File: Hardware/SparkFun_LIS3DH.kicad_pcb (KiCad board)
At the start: 2 copper layers, 25.4 x 25.4 mm, 53 parts, among them J1 Conn_01x02, J2 Conn_01x05, J3 Qwiic_RA, J4 I2C, J5 Qwiic_RA, U1 LIS3DH

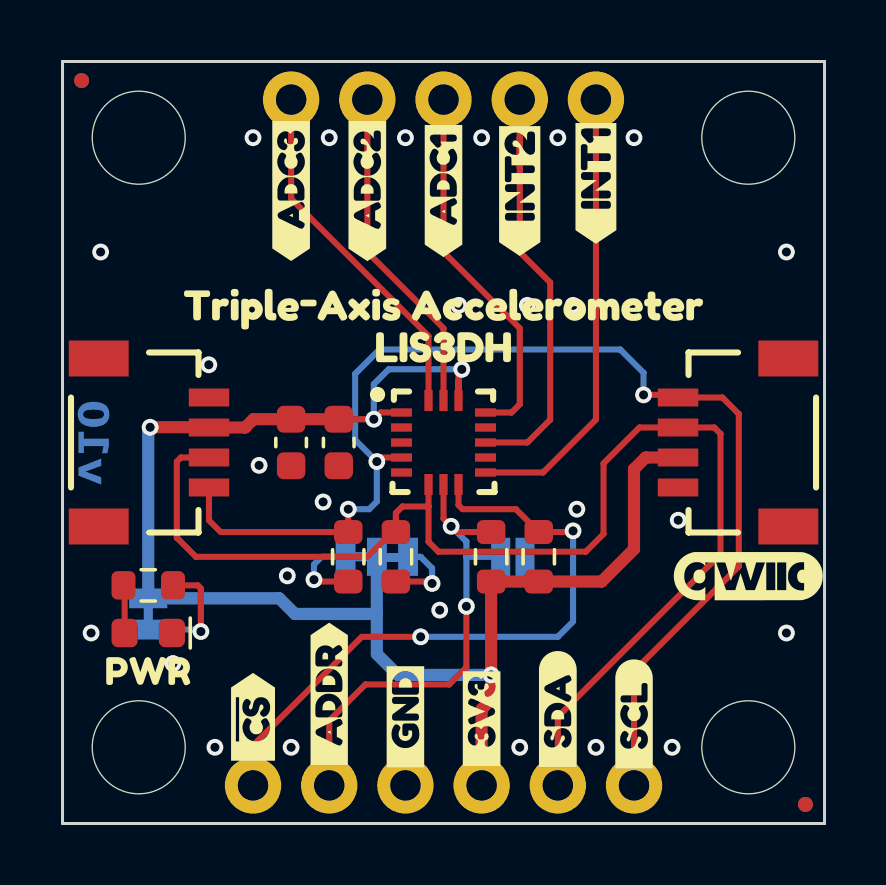
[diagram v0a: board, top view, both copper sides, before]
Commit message: Aligns the PTH for breadboard-ability
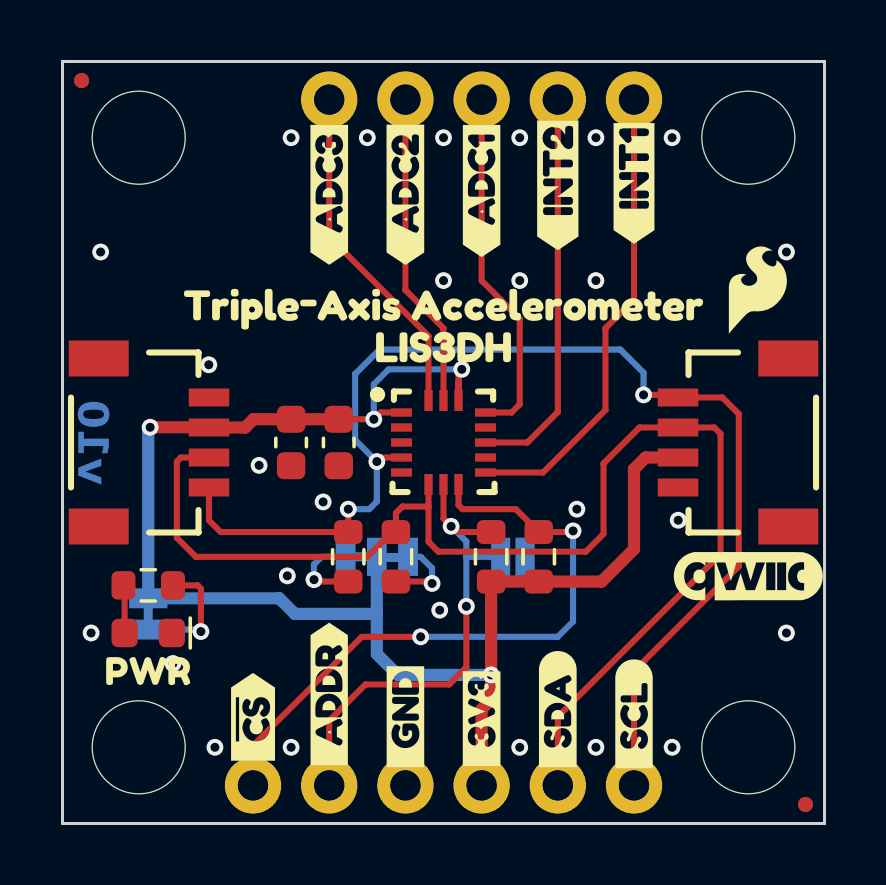
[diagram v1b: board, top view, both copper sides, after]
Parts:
- added G***: Flame, SparkFun-Aesthetic:SparkFun_Flame_3mm, F.Cu at (146.4, 93.0)
- moved kibuzzard-683879AC 1.28 mm to (139.8, 89.5)
- moved kibuzzard-68387A37 1.28 mm to (134.7, 89.9)
- moved kibuzzard-68387A3F 1.28 mm to (132.2, 89.9)
- moved J2 1.27 mm to (142.3, 86.7)
- moved kibuzzard-6838798C 1.27 mm to (142.3, 89.5)
- moved kibuzzard-68387A29 1.27 mm to (137.2, 89.7)
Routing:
- net INT1: track 14.6 -> 13.2 mm
- net INT2: track 15.1 -> 15.6 mm
- net ADC2: track 11.1 -> 10.6 mm
- net ADC1: track 11.9 -> 11.4 mm
- net ADC3: track 12.5 -> 11.9 mm

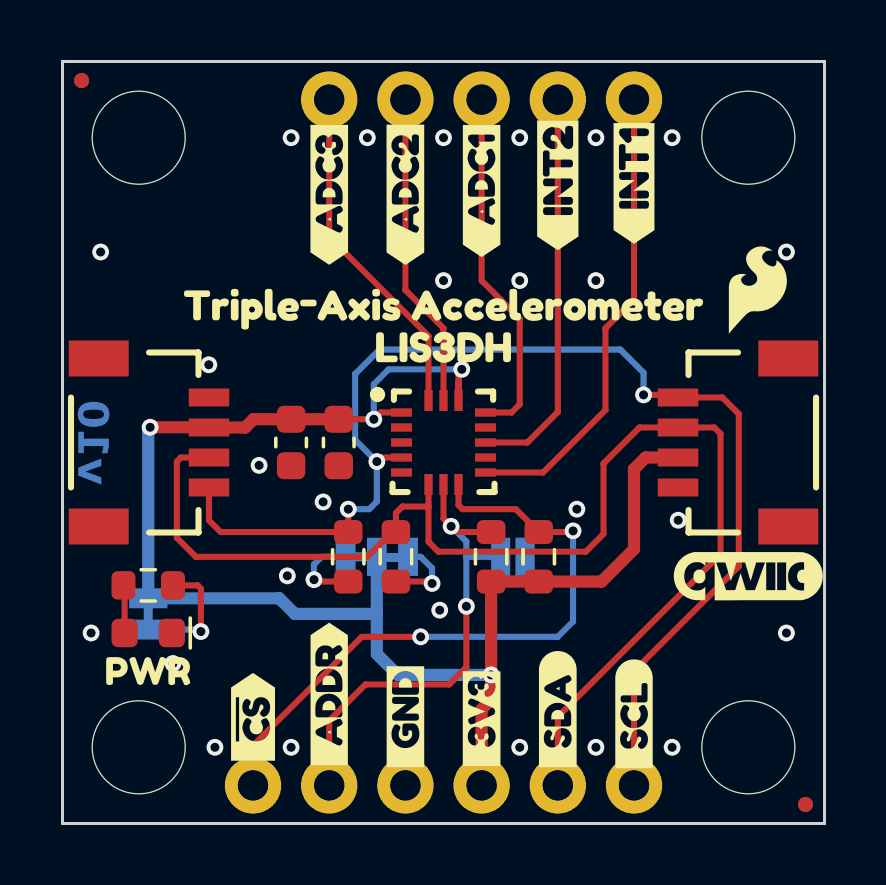
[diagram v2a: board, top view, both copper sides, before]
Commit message: Finishes schematic for mini sized version
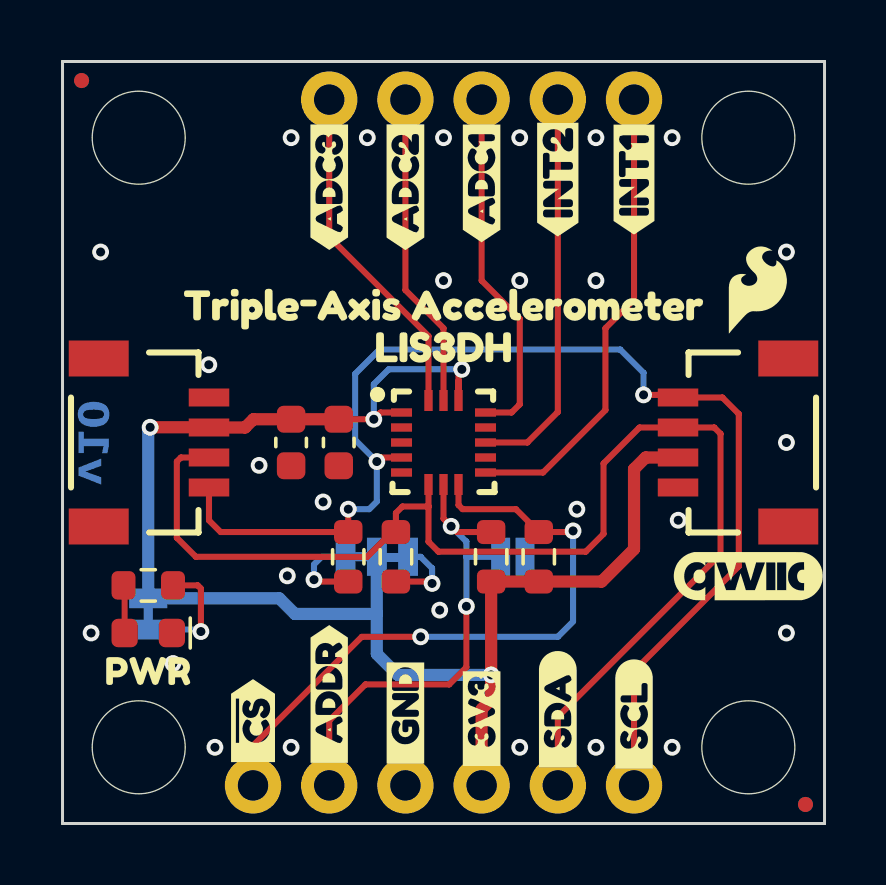
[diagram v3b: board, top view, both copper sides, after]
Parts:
- removed kibuzzard-67BF7C99: G***, kibuzzard-67BF7C99
- removed kibuzzard-67BF7CAB: G***, kibuzzard-67BF7CAB
- removed kibuzzard-67BF7CFE: G***, kibuzzard-67BF7CFE
- removed kibuzzard-67BF7D12: G***, kibuzzard-67BF7D12
- removed kibuzzard-67BF7F2F: G***, kibuzzard-67BF7F2F
- removed kibuzzard-6838798C: G***, kibuzzard-6838798C
- removed kibuzzard-683879AC: G***, kibuzzard-683879AC
- removed kibuzzard-68387A29: G***, kibuzzard-68387A29
- removed kibuzzard-68387A37: G***, kibuzzard-68387A37
- removed kibuzzard-68387A3F: G***, kibuzzard-68387A3F
- removed kibuzzard-68387A66: G***, kibuzzard-68387A66
- removed kibuzzard-68387A76: G***, kibuzzard-68387A76
- added kibuzzard-6838B6EB: G***, kibuzzard-6838B6EB, B.Cu at (141.4, 101.9)
- added kibuzzard-6838B72C: G***, kibuzzard-6838B72C, F.Cu at (139.8, 89.3)
- added kibuzzard-6838B739: G***, kibuzzard-6838B739, F.Cu at (137.2, 89.5)
- added kibuzzard-6838B744: G***, kibuzzard-6838B744, F.Cu at (134.7, 89.6)
- added kibuzzard-6838B74C: G***, kibuzzard-6838B74C, F.Cu at (132.2, 89.6)
- added kibuzzard-6838B753: G***, kibuzzard-6838B753, F.Cu at (142.3, 89.3)
- added kibuzzard-6838B970: G***, kibuzzard-6838B970, F.Cu at (129.6, 107.4)
- added kibuzzard-6838B970: G***, kibuzzard-6838B970, B.Cu at (129.7, 107.4)
- added kibuzzard-6838B976: G***, kibuzzard-6838B976, F.Cu at (132.2, 106.5)
- added kibuzzard-6838B976: G***, kibuzzard-6838B976, B.Cu at (132.2, 106.5)
- added kibuzzard-6838B97C: G***, kibuzzard-6838B97C, F.Cu at (134.7, 107.1)
- added kibuzzard-6838B980: G***, kibuzzard-6838B980, F.Cu at (137.2, 107.3)
- added kibuzzard-6838B984: G***, kibuzzard-6838B984, F.Cu at (139.8, 107.0)
- added kibuzzard-6838B988: G***, kibuzzard-6838B988, F.Cu at (142.3, 107.2)
- added kibuzzard-6838BA05: G***, kibuzzard-6838BA05, B.Cu at (139.8, 89.3)
- added kibuzzard-6838BA16: G***, kibuzzard-6838BA16, B.Cu at (142.3, 89.3)
- added kibuzzard-6838BA22: G***, kibuzzard-6838BA22, B.Cu at (132.2, 89.5)
- added kibuzzard-6838BA4A: G***, kibuzzard-6838BA4A, B.Cu at (134.7, 89.3)
- added kibuzzard-6838BA57: G***, kibuzzard-6838BA57, B.Cu at (137.2, 89.6)
- added kibuzzard-6838BBAA: G***, kibuzzard-6838BBAA, B.Cu at (142.3, 107.2)
- moved kibuzzard-67D9D97F 0.19 mm to (130.8, 101.9)
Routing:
- net GND: vias 26 -> 27

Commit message: Fixes some silk
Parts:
- removed kibuzzard-67BF7EBF: G***, kibuzzard-67BF7EBF
- removed kibuzzard-67BF7ED9: G***, kibuzzard-67BF7ED9
- removed kibuzzard-67BF7F13: G***, kibuzzard-67BF7F13
- removed kibuzzard-6838B739: G***, kibuzzard-6838B739
- removed the kibuzzard-6838B970 at (129.7, 107.4)
- removed the kibuzzard-6838B976 at (132.2, 106.5)
- removed kibuzzard-6838BA57: G***, kibuzzard-6838BA57
- added kibuzzard-68489282: G***, kibuzzard-68489282, B.Cu at (139.8, 107.0)
- added kibuzzard-6848928D: G***, kibuzzard-6848928D, B.Cu at (137.2, 107.3)
- added kibuzzard-68489296: G***, kibuzzard-68489296, B.Cu at (134.7, 107.2)
- added kibuzzard-684892AC: G***, kibuzzard-684892AC, B.Cu at (132.2, 106.5)
- added kibuzzard-684892BE: G***, kibuzzard-684892BE, B.Cu at (129.6, 107.4)
- added kibuzzard-68489319: G***, kibuzzard-68489319, F.Cu at (137.2, 89.5)
- added kibuzzard-68489323: G***, kibuzzard-68489323, B.Cu at (137.2, 89.5)
- moved G*** 1.80 mm to (135.7, 93.5)
- moved kibuzzard-6837731A 0.25 mm to (136.0, 98.4)

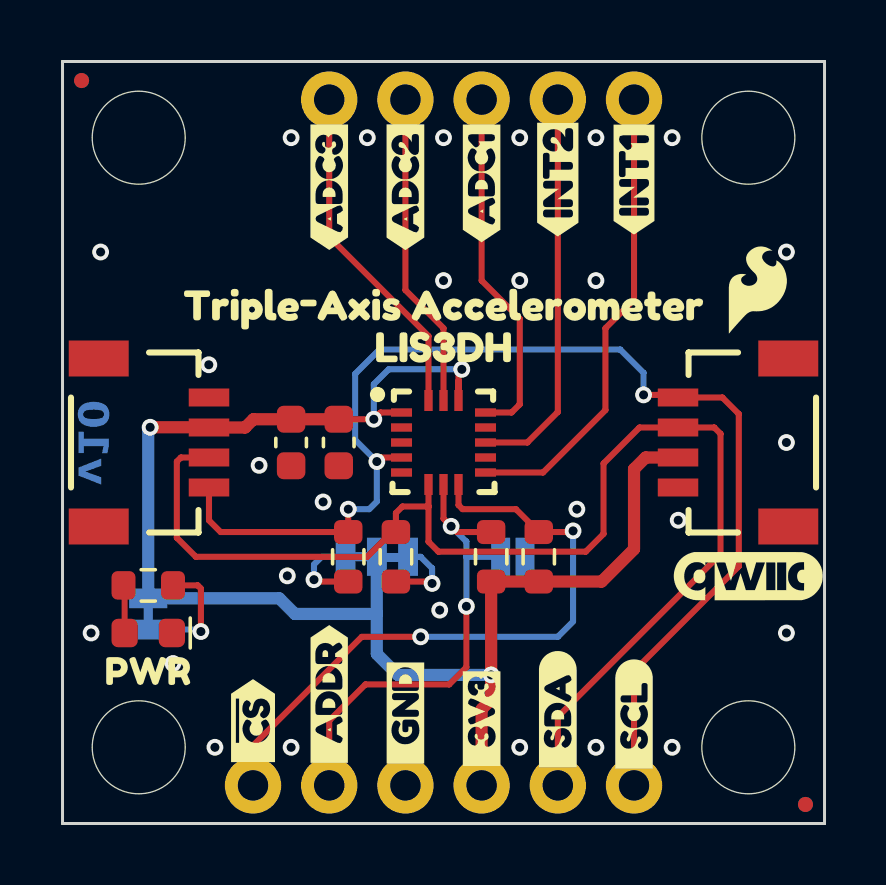
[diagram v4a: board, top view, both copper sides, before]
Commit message: Fixes LED silk
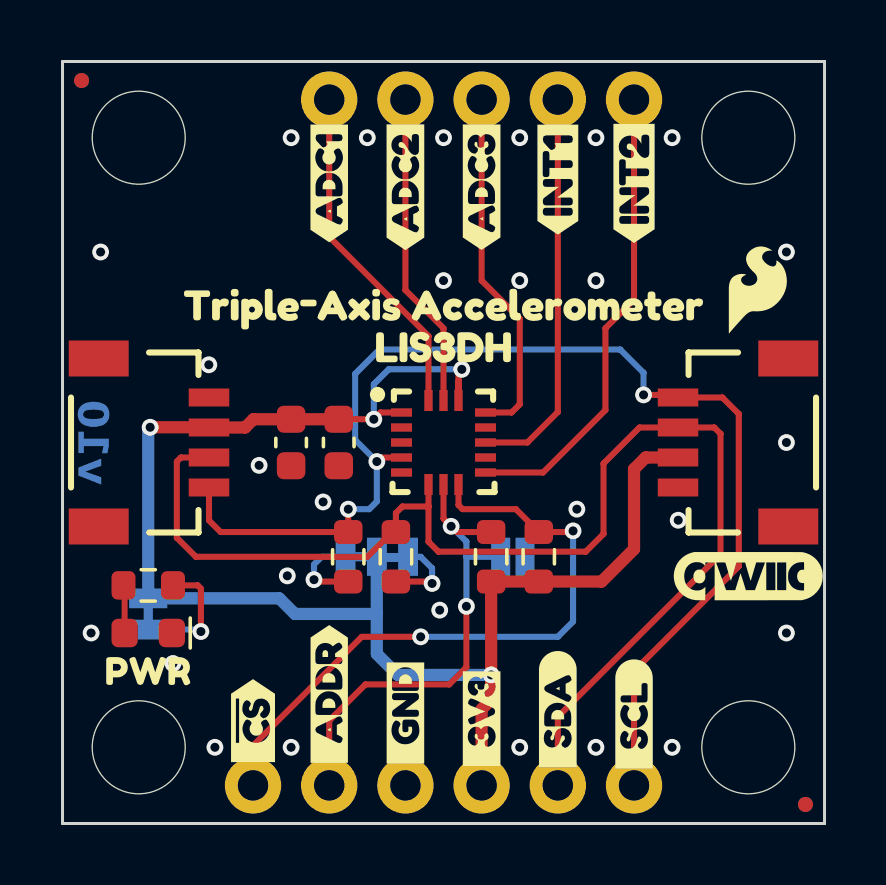
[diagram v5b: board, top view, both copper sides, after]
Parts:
- removed kibuzzard-67D9E7C1: G***, kibuzzard-67D9E7C1
- removed kibuzzard-6838B72C: G***, kibuzzard-6838B72C
- removed kibuzzard-6838B74C: G***, kibuzzard-6838B74C
- removed kibuzzard-6838B753: G***, kibuzzard-6838B753
- removed kibuzzard-6838BA05: G***, kibuzzard-6838BA05
- removed kibuzzard-6838BA16: G***, kibuzzard-6838BA16
- removed kibuzzard-6838BA22: G***, kibuzzard-6838BA22
- removed kibuzzard-68489319: G***, kibuzzard-68489319
- added kibuzzard-68489388: G***, kibuzzard-68489388, B.Cu at (132.2, 89.5)
- added kibuzzard-6848939E: G***, kibuzzard-6848939E, F.Cu at (132.2, 89.5)
- added kibuzzard-684893BE: G***, kibuzzard-684893BE, B.Cu at (142.3, 89.5)
- added kibuzzard-684893C6: G***, kibuzzard-684893C6, B.Cu at (139.8, 89.3)
- added kibuzzard-684893E9: G***, kibuzzard-684893E9, F.Cu at (142.3, 89.5)
- added kibuzzard-684893FA: G***, kibuzzard-684893FA, F.Cu at (139.8, 89.3)
- added kibuzzard-68489408: G***, kibuzzard-68489408, F.Cu at (137.2, 89.6)
- added kibuzzard-68489728: G***, kibuzzard-68489728, B.Cu at (126.2, 100.9)
- moved kibuzzard-6838BA4A 0.26 mm to (134.7, 89.6)
- moved kibuzzard-68489323 0.13 mm to (137.2, 89.6)

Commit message: Updates LIS3DH according to new changes
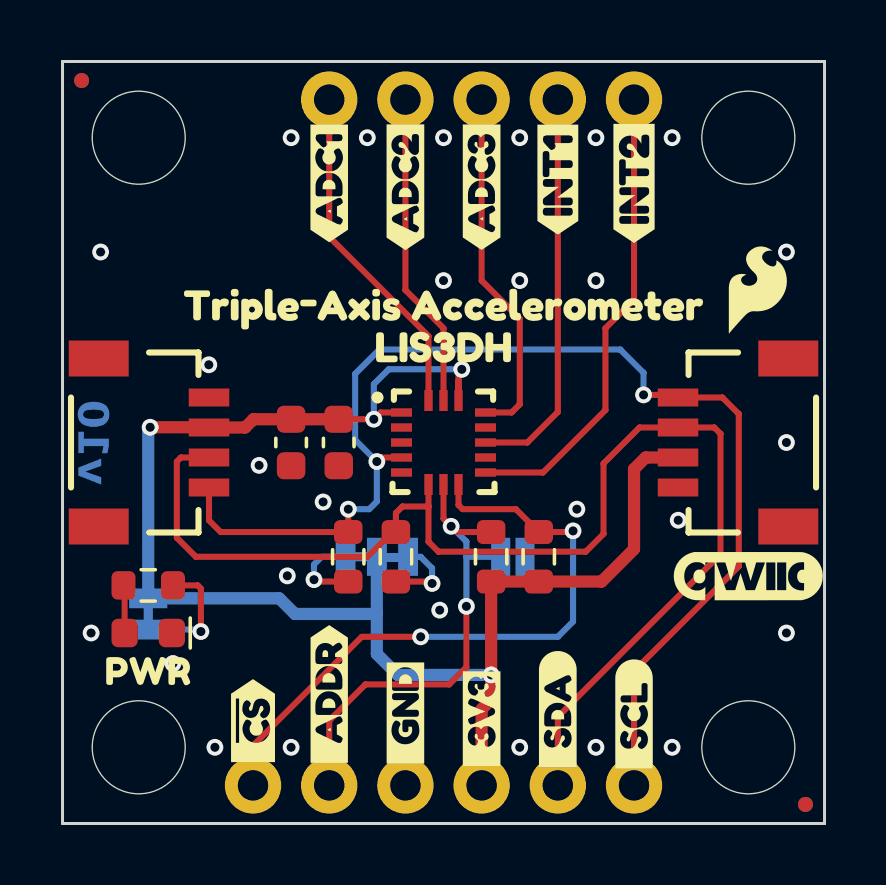
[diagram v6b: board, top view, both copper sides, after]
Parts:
- U1: footprint SparkFun-Sensor:LGA-16-3X3 -> SparkFun-Sensor:ST_LGA-16_3x3mm_P0.5mm_5x3
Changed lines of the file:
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@@
 		)
 	)
-	(footprint "SparkFun-Sensor:LGA-16-3X3"
+	(footprint "SparkFun-Sensor:ST_LGA-16_3x3mm_P0.5mm_5x3"
 		(layer "F.Cu")
 		(at 135.966 98.106)
-		(descr "16-Pin Land Grid Array (LGA) (3 x 3 mm)\n\nhttps://www.sparkfun.com/datasheets/Sensors/Accelerometer/LIS331HH.pdf Datasheet\n\nSpecifications:\n\n• Pin Count: 16\n• Area: 3.0 x 3.0 x 1.0 mm\n• Pitch: 0.5 mm\n\nDevices Using:\n\n• LIS331\n• LIS3DH")
+		(descr "ST 16-Pin Land Grid Array (LGA) (3 x 3 mm)")
+		(tags "SparkFun")
 		(property "Reference" "U1"
 			(at 0 -1.905 0)
@@
 		)
 		(fp_circle
-			(center -2.2 -1.6)
-			(end -2.073 -1.6)
+			(center -2.2 -1.5)
+			(end -2.3 -1.5)
 			(stroke
-				(width 0.254)
+				(width 0.2)
 				(type solid)
 			)
@@
 		)
 		(fp_line
+			(start -1 0)
+			(end -0.8 -0.2)
+			(stroke
+				(width 0.1)
+				(type default)
+			)
+			(layer "F.Fab")
+		)
+		(fp_line
+			(start -1 0)
+			(end -0.8 0.2)
+			(stroke
+				(width 0.1)
+				(type default)
+			)
+			(layer "F.Fab")
+		)
+		(fp_line
+			(start 0 0)
+			(end -1 0)
+			(stroke
+				(width 0.1)
+				(type default)
+			)
+			(layer "F.Fab")
+		)
+		(fp_line
+			(start 0 0)
+			(end 0 1)
+			(stroke
+				(width 0.1)
+				(type default)
+			)
+			(layer "F.Fab")
+		)
+		(fp_line
+			(start 0 1)
+			(end -0.2 0.8)
+			(stroke
+				(width 0.1)
+				(type default)
+			)
+			(layer "F.Fab")
+		)
+		(fp_line
+			(start 0 1)
+			(end 0.2 0.8)
+			(stroke
+				(width 0.1)
+				(type default)
+			)
+			(layer "F.Fab")
+		)
+		(fp_line
 			(start 1.5 -1.5)
 			(end 1.5 1.5)
@@
 			(layer "F.Fab")
 		)
+		(fp_circle
+			(center 0 0)
+			(end -0.25 0)
+			(stroke
+				(width 0.1)
+				(type default)
+			)
+			(fill no)
+			(layer "F.Fab")
+		)
+		(fp_circle
+			(center 0 0)
+			(end -0.05 0)
+			(stroke
+				(width 0.1)
+				(type default)
+			)
+			(fill no)
+			(layer "F.Fab")
+		)
+		(fp_text user "Z"
+			(at 0.4 -0.35 0)
+			(unlocked yes)
+			(layer "F.Fab")
+			(effects
+				(font
+					(size 0.25 0.25)
+					(thickness 0.0625)
+				)
+			)
+		)
+		(fp_text user "X"
+			(at -0.8 -0.5 0)
+			(unlocked yes)
+			(layer "F.Fab")
+			(effects
+				(font
+					(size 0.25 0.25)
+					(thickness 0.0625)
+				)
+			)
+		)
+		(fp_text user "Y"
+			(at 0.25 0.5 0)
+			(unlocked yes)
+			(layer "F.Fab")
+			(effects
+				(font
+					(size 0.25 0.25)
+					(thickness 0.0625)
+				)
+			)
+		)
 		(pad "1" smd rect
 			(at -1.4 -1 180)
@@
 		)
 		(embedded_fonts no)
-		(model "${SPARKFUN_KICAD_LIBRARY}/Footprints/SparkFun-3D-models/Sensor/LIS3DH_LGA-16_3x3x1mm.step"
+		(model "${SPARKFUN_KICAD_LIBRARY}/Footprints/SparkFun-3D-models/Semiconductor-Standard/LGA-16_3x3x1mm.step"
 			(offset
 				(xyz 0 0 0)
@@
 				(font
 					(size 0.001 0.001)
+					(thickness 0.15)
 				)
 			)
@@
 				(font
 					(size 0.001 0.001)
+					(thickness 0.15)
 				)
 			)
@@
 				(font
 					(size 0.001 0.001)
+					(thickness 0.15)
 				)
 			)
@@
 				(font
 					(size 0.001 0.001)
+					(thickness 0.15)
 				)
 			)
@@
 				(font
 					(size 0.001 0.001)
+					(thickness 0.15)
 				)
 			)
@@
 				(font
 					(size 0.001 0.001)
+					(thickness 0.15)
 				)
 			)
@@
 				(font
 					(size 0.001 0.001)
+					(thickness 0.15)
 				)
 			)
@@
 				(font
 					(size 0.001 0.001)
+					(thickness 0.15)
 				)
 			)
@@
 				(font
 					(size 0.001 0.001)
+					(thickness 0.15)
 				)
 				(justify mirror)
@@
 				(font
 					(size 0.001 0.001)
+					(thickness 0.15)
 				)
 				(justify mirror)
@@
 				(font
 					(size 0.001 0.001)
+					(thickness 0.15)
 				)
 				(justify mirror)
@@
 				(font
 					(size 0.001 0.001)
+					(thickness 0.15)
 				)
 				(justify mirror)
@@
 				(font
 					(size 0.001 0.001)
+					(thickness 0.15)
 				)
 				(justify mirror)
@@
 				(font
 					(size 0.001 0.001)
+					(thickness 0.15)
 				)
 				(justify mirror)
@@
 				(font
 					(size 0.001 0.001)
+					(thickness 0.15)
 				)
 				(justify mirror)
@@
 				(font
 					(size 0.001 0.001)
+					(thickness 0.15)
 				)
 				(justify mirror)
@@
 				(font
 					(size 0.001 0.001)
+					(thickness 0.15)
 				)
 				(justify mirror)
@@
 				(font
 					(size 0.001 0.001)
+					(thickness 0.15)
 				)
 				(justify mirror)
@@
 				(font
 					(size 0.001 0.001)
+					(thickness 0.15)
 				)
 				(justify mirror)
@@
 				(font
 					(size 0.001 0.001)
+					(thickness 0.15)
 				)
 				(justify mirror)
@@
 				(font
 					(size 0.001 0.001)
+					(thickness 0.15)
 				)
 				(justify mirror)
@@
 				(font
 					(size 0.001 0.001)
+					(thickness 0.15)
 				)
 				(justify mirror)
@@
 				(font
 					(size 0.001 0.001)
+					(thickness 0.15)
 				)
 				(justify mirror)
@@
 				(font
 					(size 0.001 0.001)
+					(thickness 0.15)
 				)
 				(justify mirror)
@@
 				(font
 					(size 0.001 0.001)
+					(thickness 0.15)
 				)
 				(justify mirror)
@@
 				(font
 					(size 0.001 0.001)
+					(thickness 0.15)
 				)
 				(justify mirror)
@@
 				(font
 					(size 0.001 0.001)
+					(thickness 0.15)
 				)
 				(justify mirror)
@@
 				(font
 					(size 0.001 0.001)
+					(thickness 0.15)
 				)
 				(justify mirror)
